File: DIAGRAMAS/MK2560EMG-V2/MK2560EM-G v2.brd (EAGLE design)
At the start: 102.5 x 86.4 mm, 76 parts, among them U1 X-MOTOR, U2 Y-MOTOR, U3 Z-MOTOR

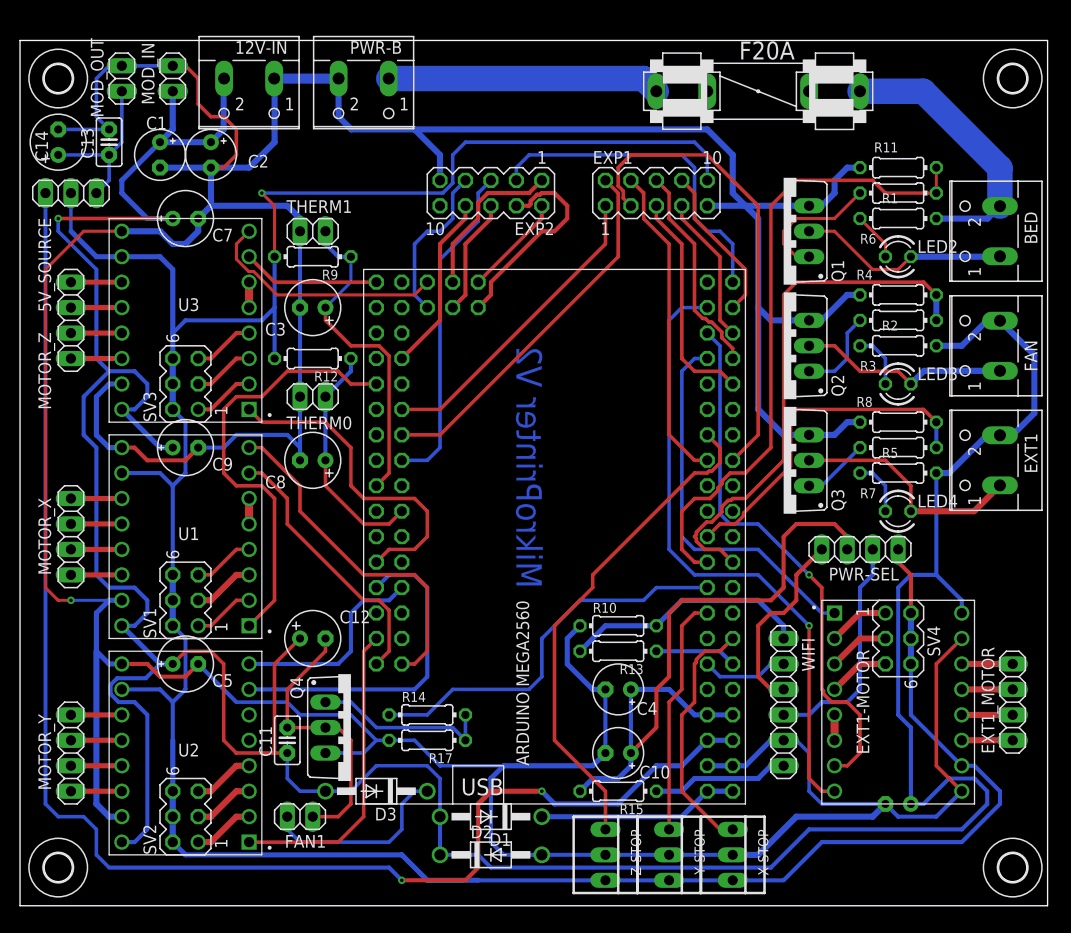
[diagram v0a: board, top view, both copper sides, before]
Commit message: pcb minor fix
- optimization and minor pcb fix for better design and perfomance.
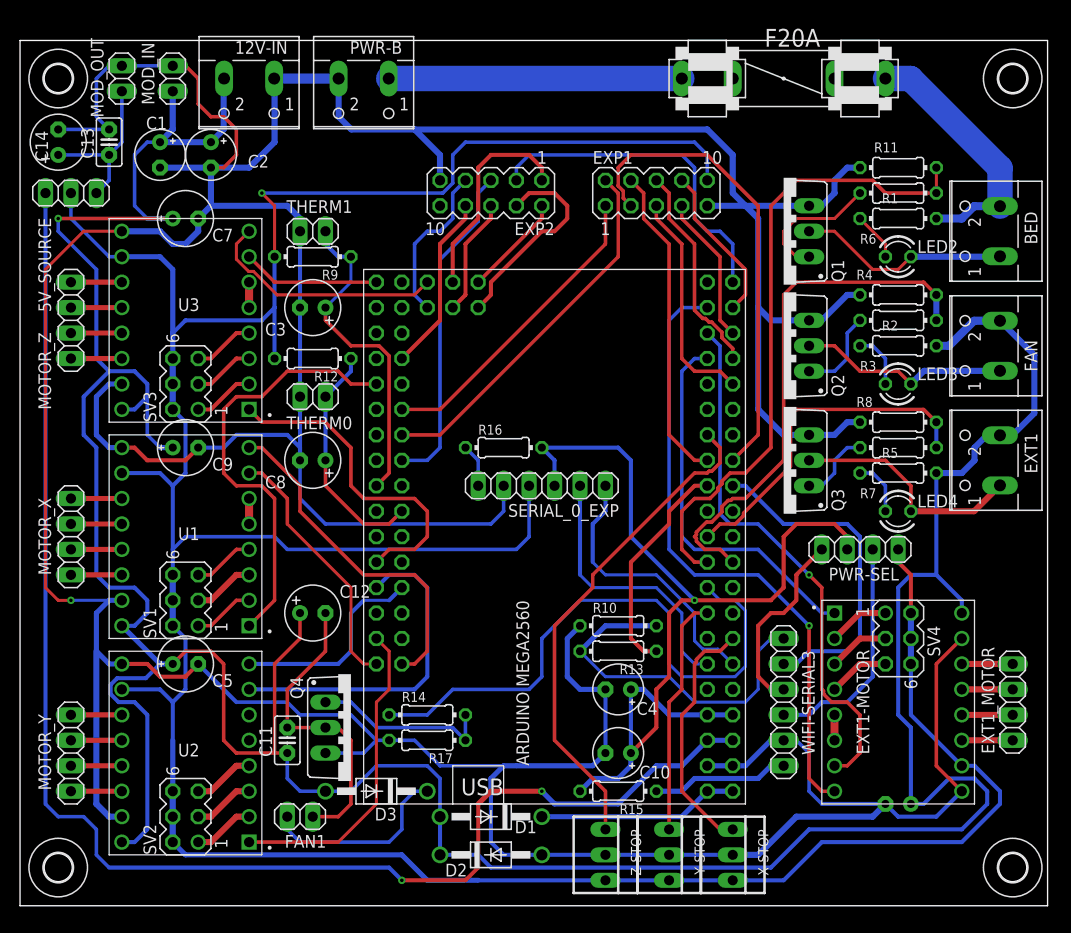
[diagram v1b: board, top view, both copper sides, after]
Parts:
- added R16: 10k, resistor:0204/7
- added SERIAL_0_EXP: g+5v3v3rxtx, pinhead:1X06
- moved F20A 2.84 mm to (77.5, 74.9)
- moved C12 2.54 mm to (30.5, 21.6)
- renumbered WIFI to WIFI-SERIAL3
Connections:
- new net CH-PD: R16.1, SERIAL_0_EXP.6
- net +3V3.2: now also R16.2, SERIAL_0_EXP.3
- net +5V: now also SERIAL_0_EXP.4
- net D1: now also SERIAL_0_EXP.2; no longer WIFI-SERIAL3.2
- net D2: now also SERIAL_0_EXP.1; no longer R13.1
- net GND: now also SERIAL_0_EXP.5
- net RX3: now also WIFI-SERIAL3.2
- net TX3: now also R13.1
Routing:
- net +5V: track 284.4 -> 325.9 mm
- net RX3: track 0.00 -> 33.6 mm
- net +3V3.2: track 66.7 -> 97.1 mm, vias 0 -> 1
- net GND: track 516.6 -> 545.6 mm
- net TX3: track 0.00 -> 22.2 mm
- net FAN-CTRL: track 39.2 -> 59.4 mm
- net D2: track 8.15 -> 27.9 mm
- net D1: track 8.67 -> 27.5 mm
- net N$18: track 24.7 -> 36.0 mm
- net +12V5A: track 339.9 -> 345.6 mm
- net D50: track 16.3 -> 21.2 mm
- net CH-PD: track 0.00 -> 4.34 mm
- net FAN-V: track 29.3 -> 31.8 mm
- net N$29: track 27.2 -> 29.2 mm
- net +12V: track 27.8 -> 25.9 mm
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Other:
- board text removed: "MikroPrinter V2"

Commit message: new pcb files
- updated pcb and sch files!
- new improvements and funcionality of the controller board.
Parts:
- added C15, C16, C17: (no value), capacitor-wima:C2.5-2
- added C19, C20, C21: 470uf, rcl:E2,5-6E
- added FIL-SENS: (no value), -redpic-connector:1X03
- added Q5, Q6, Q7: 5.8A/30V/35mΩ, SparkFun-DiscreteSemi:SOT23-3
- added R18, R19, R20, R21, R22, R23: 10k, resistor:0204/7
- added RGB-LANES: (no value), -redpic-connector:1X04
- moved F20A 21.6 mm to (55.9, 73.7)
- moved R16 4.02 mm to (50.8, 34.3)
- moved SERIAL_0_EXP 3.81 mm to (53.3, 30.5)
- moved EXT1_MOTOR 1.27 mm to (100.3, 11.4)
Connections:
- new net B-LED: Q7.1, R20.2
- new net FILM-SENS: ARD-MEGA.D5, FIL-SENS.1
- new net G-LED: Q6.1, R19.2
- new net L-B: C17.1, C21.+, Q7.3, RGB-LANES.3
- new net L-G: C16.1, C19.+, Q6.3, RGB-LANES.2
- new net L-R: C15.1, C20.+, Q5.3, RGB-LANES.1
- new net R-LED: Q5.1, R18.2
- net +5V: now also FIL-SENS.3
- net D43: now also R18.1, R21.1
- net D44: now also R19.1, R22.1
- net D45: now also R20.1, R23.1
- net GND: now also C15.2, C16.2, C17.2, C19.-, C20.-, C21.-, FIL-SENS.2, Q5.2, Q6.2, Q7.2, R21.2, R22.2, R23.2, RGB-LANES.4
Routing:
- net GND: track 545.6 -> 665.6 mm
- net L-B: track 0.00 -> 52.3 mm, vias 0 -> 1
- net L-R: track 0.00 -> 46.3 mm
- net L-G: track 0.00 -> 43.4 mm
- net FILM-SENS: track 0.00 -> 25.7 mm
- net N$29: track 29.2 -> 8.19 mm
- net +12V: track 25.9 -> 46.9 mm
- net D44: track 0.00 -> 19.5 mm
- net D43: track 0.00 -> 9.20 mm
- net D45: track 0.00 -> 7.40 mm
- net +3V3.2: track 97.1 -> 90.0 mm
- net D33: track 33.1 -> 39.4 mm
- net D2: track 27.9 -> 22.3 mm
- net D49: track 16.1 -> 21.6 mm
- net Z-MIN: track 49.7 -> 45.5 mm
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
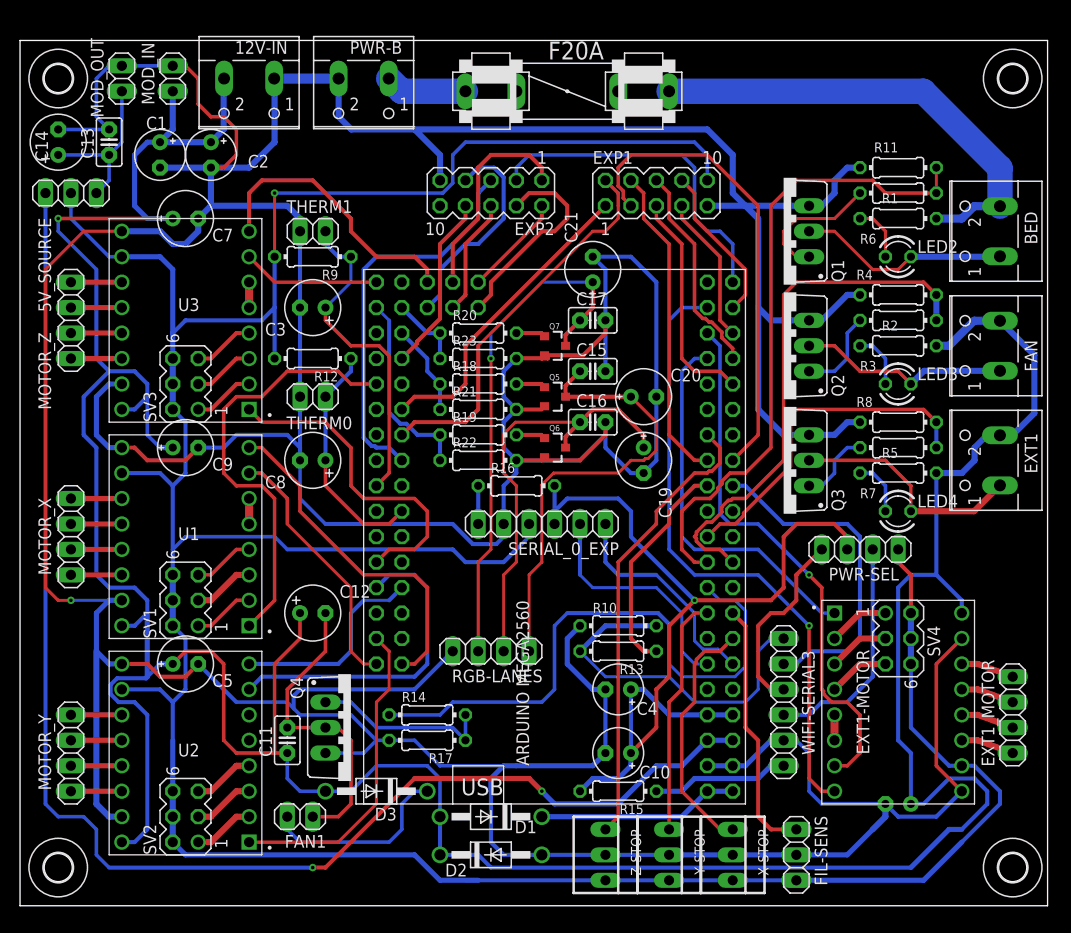
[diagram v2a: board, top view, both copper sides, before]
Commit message: important pcb update
- added XT60 connectors for bed connection.
- optimization of some pcb tracks, added support for ext reset button.
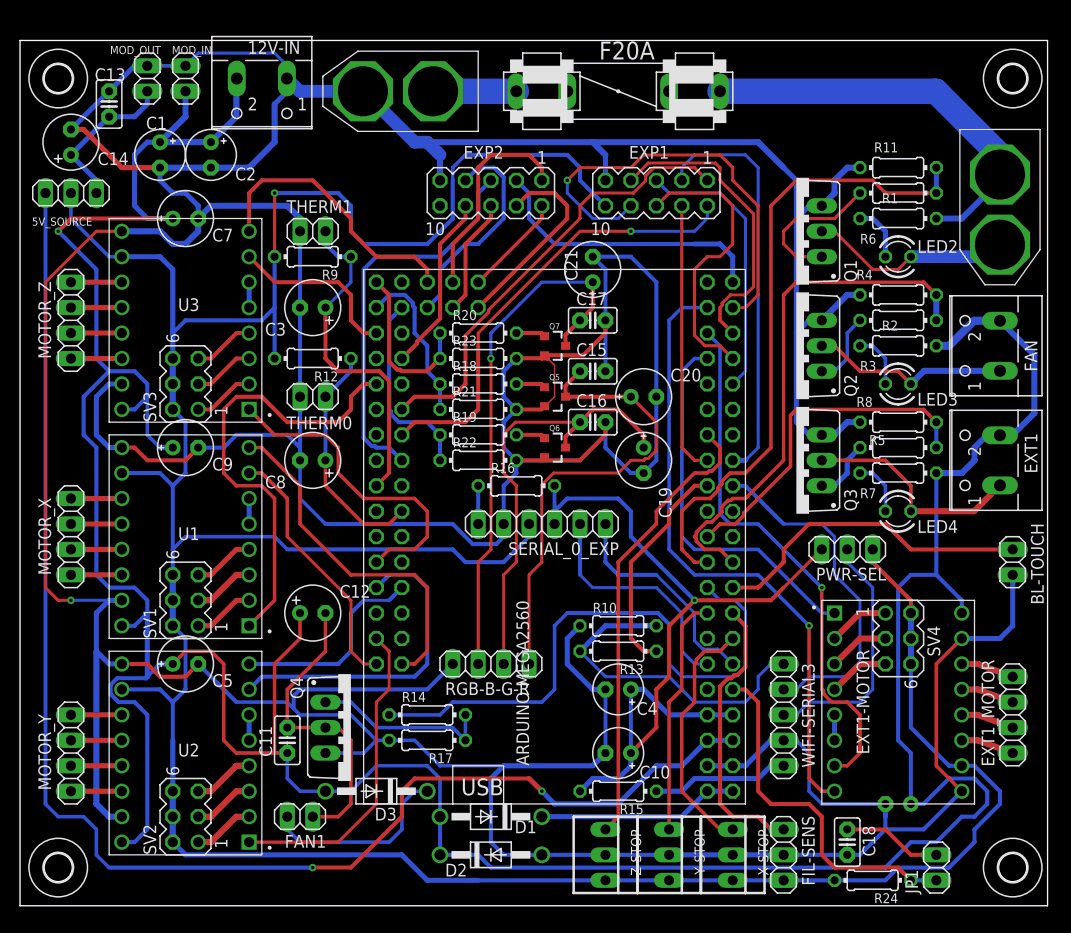
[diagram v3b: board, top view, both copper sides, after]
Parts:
- removed BED, PWR-B: (no value), con-wago-500:W237-102
- removed RGB-LANES: (no value), -redpic-connector:1X04
- added BL-TOUCH, JP1: (no value), -redpic-connector:1X02
- added C18: 100nF, capacitor-wima:C2.5-2
- added R24: 10k, resistor:0204/7
- added RGB-B-G-R: (no value), -redpic-connector:1X04
- added U$1, U$2: XT60, XT60:XT60
- C15, C16, C17: value (none) -> 100nF
- PWR-SEL: device -redpic-connector:1X04 -> -redpic-connector:1X03
- R18, R19, R20: value 10k -> 4k7
- WIFI-SERIAL3: device pinhead:1X06 -> pinhead:1X05
- moved F20A 5.08 mm to (61.0, 73.7)
- moved C13 3.81 mm to (10.2, 72.4)
- moved MOD_OUT 2.54 mm to (14.0, 74.9)
- moved PWR-SEL 1.27 mm to (83.8, 27.9)
- moved 12V-IN 1.27 mm to (25.4, 73.7)
- moved C14 1.27 mm to (6.35, 68.6)
- moved MOD_IN 1.27 mm to (17.8, 74.9)
- moved WIFI-SERIAL3 1.27 mm to (77.5, 11.4)
- moved FIL-SENS 1.27 mm to (77.5, -2.54)
- moved Q1 1.27 mm to (78.7, 59.7)
- moved Q2 1.27 mm to (78.7, 48.3)
- moved Q3 1.27 mm to (78.7, 36.8)
- turned EXP1 to 180 degrees
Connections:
- removed net D42: ARD-MEGA.D42
- removed net N$31: PWR-SEL.2, WIFI-SERIAL3.4
- new net D46: ARD-MEGA.D46, R20.1, R23.1
- new net D7: ARD-MEGA.D7, BL-TOUCH.1
- new net N$33: C18.1, JP1.2
- net +12V: now also U$2.+; no longer BED.2
- net +5V: now also R24.2
- net CH_PD: now also WIFI-SERIAL3.5; no longer WIFI-SERIAL3.6
- net D43: no longer R18.1, R21.1
- net D44: now also R18.1, R21.1; no longer R19.1, R22.1
- net D45: now also R19.1, R22.1; no longer R20.1, R23.1
- net GND: now also BL-TOUCH.2, C18.2, RGB-B-G-R.4, U$1.-, WIFI-SERIAL3.4; no longer PWR-B.2, RGB-LANES.4, WIFI-SERIAL3.5
- net L-B: now also RGB-B-G-R.3; no longer RGB-LANES.3
- net L-G: now also RGB-B-G-R.2; no longer RGB-LANES.2
- net L-R: now also RGB-B-G-R.1; no longer RGB-LANES.1
- net N$29: now also U$1.+; no longer PWR-B.1
- net N$32: now also PWR-SEL.2; no longer PWR-SEL.4
- net N$7: now also U$2.-; no longer BED.1
- net RESET: now also JP1.1, R24.1
- net Z-STEP: now also ARD-MEGA.D42; no longer ARD-MEGA.D46
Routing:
- net RESET: track 0.00 -> 35.7 mm
- net D7: track 0.00 -> 32.4 mm
- net D29: track 15.9 -> 44.1 mm, vias 0 -> 1
- net N$31: track 23.2 -> 0.00 mm
- net D46: track 0.00 -> 17.0 mm
- net D27: track 14.8 -> 30.5 mm
- net D37: track 31.0 -> 45.0 mm
- net D45: track 7.40 -> 19.5 mm
- net N$33: track 0.00 -> 9.94 mm
- net D43: track 9.20 -> 0.00 mm
- net D25: track 21.2 -> 28.7 mm
- net +3V3.2: track 90.0 -> 82.9 mm
- net GND: track 665.6 -> 672.6 mm
- net D35: track 38.6 -> 45.2 mm, vias 0 -> 1
- net D17: track 47.4 -> 40.9 mm
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
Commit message: new pcb update and fixes
- new pcb fixes and testing for factory pcb production.
- added picture of pcb components in place.
- added pdf with the final design of the pcb.
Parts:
- Q5, Q7: value 5.8A/30V/35mΩ -> IRML2502
- Q6: value 5.8A/30V/35mΩ -> IRLML2502
- moved EXT1_MOTOR 1.27 mm to (100.3, 12.7)
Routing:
- net +12V5A: track 347.1 -> 345.3 mm
- net +3V3.2: track 82.9 -> 84.6 mm
- net Z-MIN: track 45.5 -> 47.1 mm
- net FAN-V: track 31.8 -> 30.6 mm
- net THERM1: track 35.1 -> 33.9 mm
- net E0-STEP: track 53.8 -> 54.8 mm
- net FAN-CTRL: track 59.2 -> 60.1 mm
- net GND: track 672.6 -> 673.5 mm
- net D10: track 34.3 -> 35.2 mm
- net +5V: track 320.3 -> 319.5 mm
- net AM-VIN: track 20.1 -> 20.8 mm
- net D2: track 22.3 -> 23.0 mm
- net D9: track 52.9 -> 53.5 mm
- net D25: track 28.7 -> 29.3 mm
